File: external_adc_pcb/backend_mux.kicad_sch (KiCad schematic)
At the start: 4 parts, among them U4 TPW4051-QF4R, U5 TPW4051-QF4R

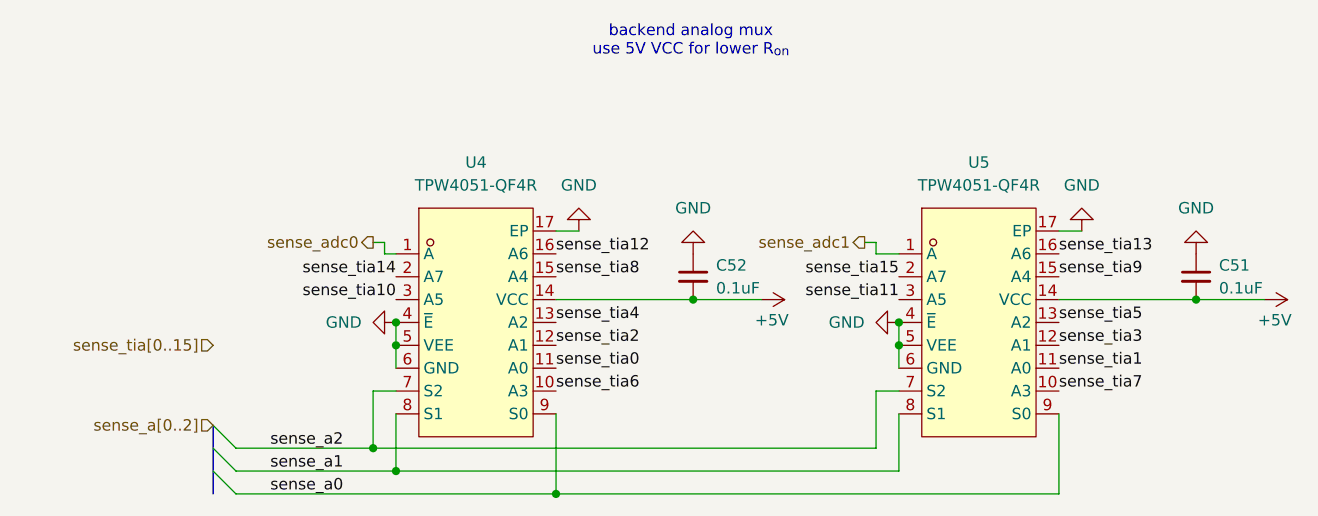
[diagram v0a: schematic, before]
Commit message: capitalize netnames; change and embed font
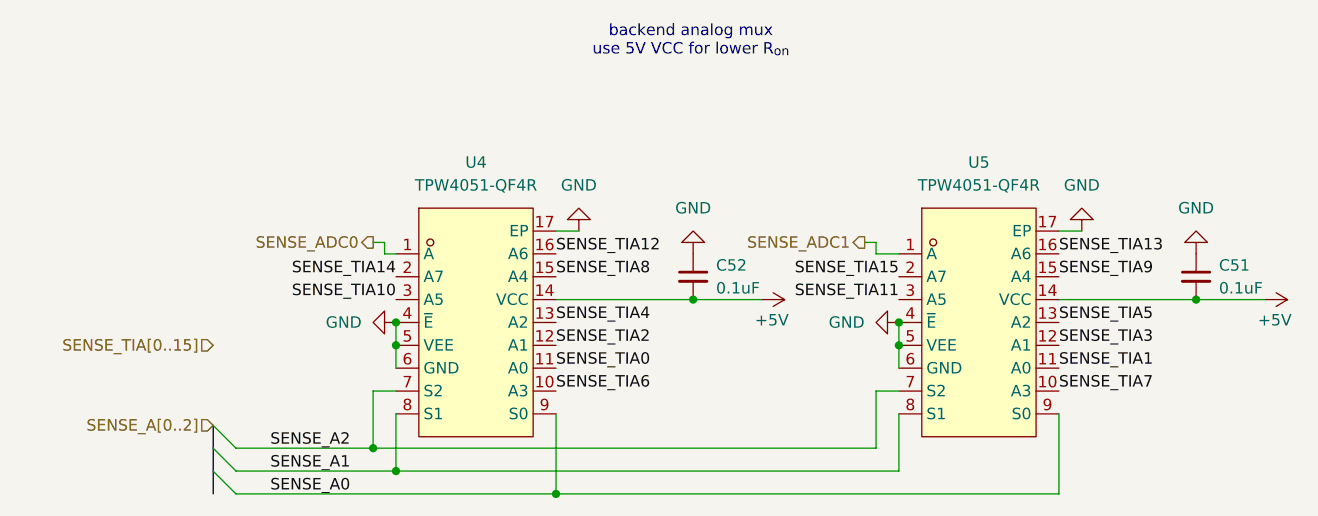
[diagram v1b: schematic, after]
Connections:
- net sense_a0 renamed SENSE_A0
- net sense_a1 renamed SENSE_A1
- net sense_a2 renamed SENSE_A2
- net sense_adc0 renamed SENSE_ADC0
- net sense_adc1 renamed SENSE_ADC1
- net sense_tia0 renamed SENSE_TIA0
- net sense_tia1 renamed SENSE_TIA1
- net sense_tia10 renamed SENSE_TIA10
- net sense_tia11 renamed SENSE_TIA11
- net sense_tia12 renamed SENSE_TIA12
- net sense_tia13 renamed SENSE_TIA13
- net sense_tia14 renamed SENSE_TIA14
- net sense_tia15 renamed SENSE_TIA15
- net sense_tia2 renamed SENSE_TIA2
- net sense_tia3 renamed SENSE_TIA3
- net sense_tia4 renamed SENSE_TIA4
- net sense_tia5 renamed SENSE_TIA5
- net sense_tia6 renamed SENSE_TIA6
- net sense_tia7 renamed SENSE_TIA7
- net sense_tia8 renamed SENSE_TIA8
- net sense_tia9 renamed SENSE_TIA9
